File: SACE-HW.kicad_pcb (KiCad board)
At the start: 2 copper layers, 76 parts, among them IC201 1769205241, J201 Header_Male_Pin_2.54mm_1X2_,_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, J202 PJ-082BH, J301 Header_Male_Pin_2.54mm_1X6_,_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, J302 XH-4A connector, J401 1935161, J402 Header_Male_Pin_2.54mm_1X3_,_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, J403 RF1-01K-D-00-50-BK-HDW, J404 1935161, J501 690-005-299-043, Q401 MCB90N12A-TP, Q402 MCB90N12A-TP, SW301 PTS645SM43SMTR92, SW302 PTS645SM43SMTR92, U201 OKI-78SR-5_1.5-W36H-C, U202 AZ1117IH-3.3TRG1, U203 AZ1117IH-3.3TRG1, U301 STM32F446RE, U401 LTV-816S, U402 TMCS1108A4UQDR, U501 MCP2221A-I_SL

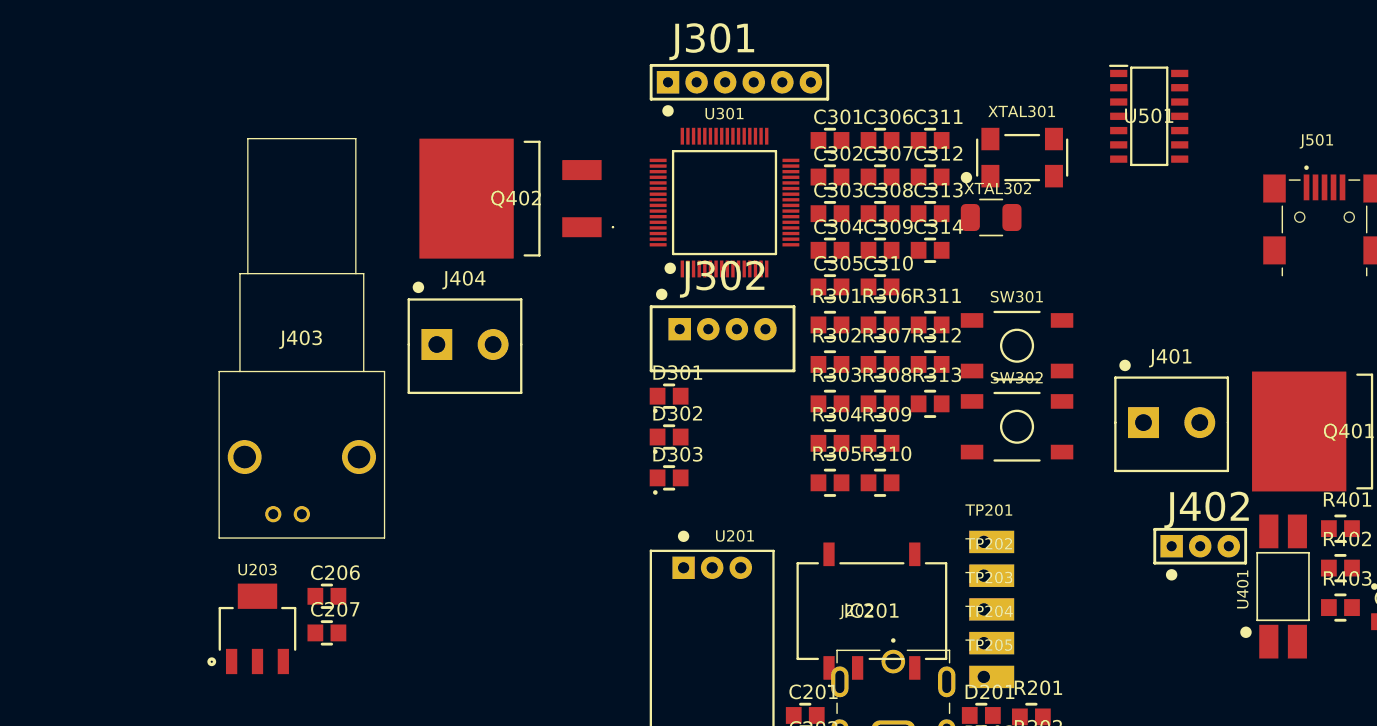
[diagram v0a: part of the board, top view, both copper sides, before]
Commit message: update schematic
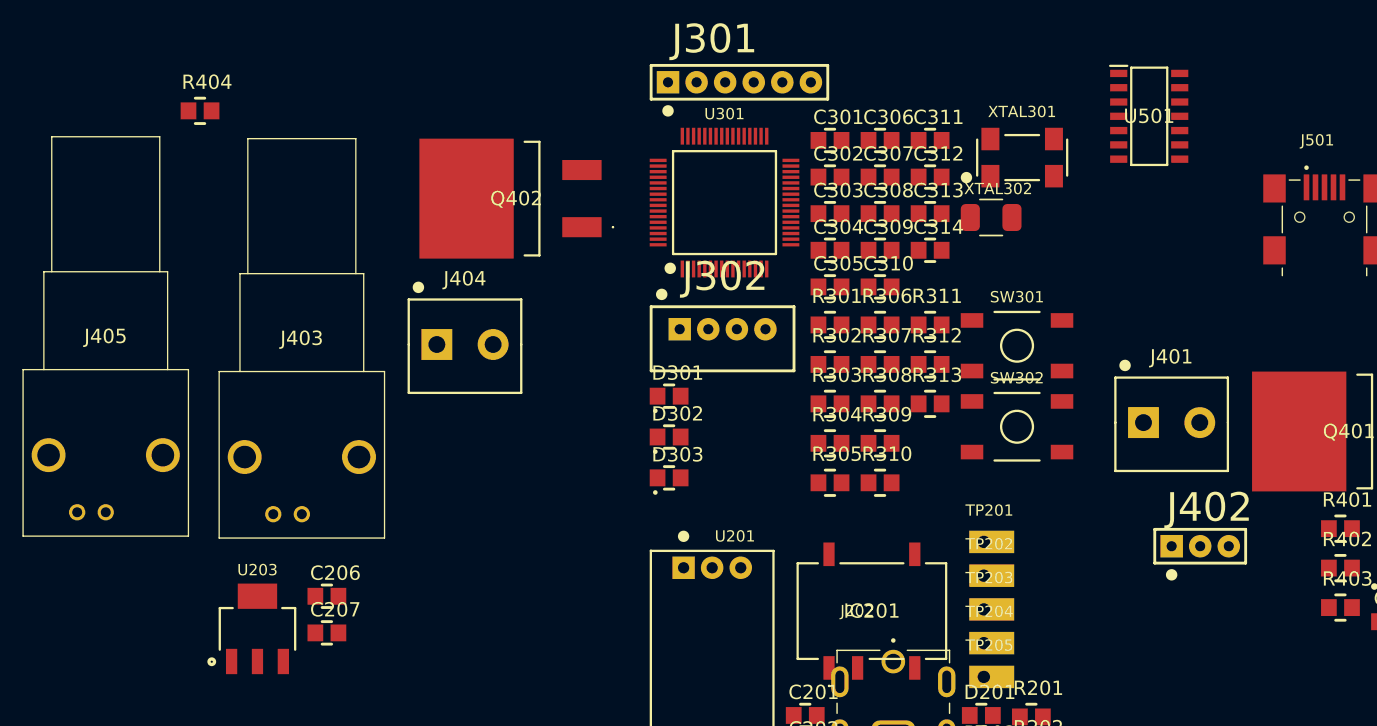
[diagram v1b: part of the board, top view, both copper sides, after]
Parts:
- removed U401: LTV-816S, IC:4-SMD
- added J405: RF1-01K-D-00-50-BK-HDW, Connectors:RF101KD0050, F.Cu at (65.2, 81.4)
- added R404: RC0805JR-071KL, Resistors:R0805, F.Cu at (72.6, 45.7)
- R401: value RC0805JR-071KL -> RC0805JR-07330RL
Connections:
- net Net-(U401-E) renamed /HV/pulse_gate
- C401 pad 2: 3.3VB -> 3.3VA
- J403 pad 2: Net-(Q402-D) -> GNDA
- J403 pad MH: Net-(Q402-D) -> GNDA
- J404 pad 1: Net-(Q402-D) -> GNDA
- Q401 pad 1: unconnected-(Q401-G-Pad1) -> Net-(Q401-G)
- Q402 pad 2: Net-(Q402-D) -> GNDA
- R401 pad 1: Net-(U401-Anode) -> /HV/boost_gate
- R401 pad 2: /HV/gate_drive -> Net-(Q401-G)
- U402 pad 5: GNDB -> GNDA
- U402 pad 8: 3.3VB -> 3.3VA
- U501 pad 5: /USB_Serial/UART_RX -> unconnected-(U501-URX-Pad5)
- U501 pad 6: /USB_Serial/UART_TX -> unconnected-(U501-UTX-Pad6)

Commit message: update schematic
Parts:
- removed U402: TMCS1108A4UQDR, IC:SOIC-8
- added C601: 885012107015, Capacitors:C0603, F.Cu at (160.4, 129.1)
- added C602: 885012107015, Capacitors:C0603, F.Cu at (160.4, 131.6)
- added C603: 885012107015, Capacitors:C0603, F.Cu at (160.4, 134.1)
- added D401: SBRD10200TR, Diodes:DPAK228P1005X240-4N, F.Cu at (91.2, 100.6)
- added J601: 2350514-8, Connectors:CONN8_2350514-8_TEC, F.Cu at (119.5, 127.0)
- added J602: XH-4A connector, Connectors:XH-4A, F.Cu at (162.7, 123.6)
- added J701: 2350514-8, Connectors:CONN8_2350514-8_TEC, F.Cu at (89.1, 127.0)
- added L401: ATCA-08-471M-H, Inductors:IND_ATCA-08-471M-H, F.Cu at (64.5, 116.8)
- added R601: RC0805JR-070RL, Resistors:R0603, F.Cu at (173.5, 129.2)
- added R602: RC0805JR-070RL, Resistors:R0603, F.Cu at (173.5, 131.9)
- added R603: RC0805JR-074K7L, Resistors:R0805, F.Cu at (164.1, 129.7)
- added R604: RC0805JR-074K7L, Resistors:R0805, F.Cu at (164.1, 133.2)
- added TP206: Test_Point_THM, Connectors:Keystone_5001, F.Cu at (151.4, 120.7)
- added U401: TMCS1108A4UQDR, IC:SOIC-8, F.Cu at (91.1, 111.6)
- added U601: TLA2528IRTER, IC:QFN50P300X300X80-17N-D, F.Cu at (170.0, 130.6)
- R402: value RC0805JR-07330RL -> RC0805JR-071KL
- R403: value RC0805JR-071KL -> RC0805JR-07330RL
- moved J202 29.7 mm to (164.2, 110.5)
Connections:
- J403 pad 2: GNDA -> /HV/electrode
- J403 pad MH: GNDA -> /HV/electrode
- J404 pad 1: GNDA -> /HV/electrode
- Q401 pad 2: unconnected-(Q401-D-Pad2) -> Net-(Q401-D)
- Q402 pad 2: GNDA -> /HV/electrode
- R402 pad 1: /HV/pulse_gate -> GNDA
- R402 pad 2: Net-(Q402-G) -> /HV/boost_gate
- R403 pad 1: GNDA -> /HV/pulse_gate
- R403 pad 2: /HV/pulse_gate -> Net-(Q402-G)
- R404 pad 2: /HV/boost_gate -> /HV/pulse_gate
- U501 pad 10: /USB_Serial/SCL -> unconnected-(U501-SCL-Pad10)
- U501 pad 9: /USB_Serial/SDA -> unconnected-(U501-SDA-Pad9)

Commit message: modif schématique
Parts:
- removed IC201: 1769205241, IC:1769205241
- added C208: 885012107014, Capacitors:C0805, F.Cu at (79.4, 125.4)
- added D204: 150080VS75000, Diodes:LED_0805_GREEN, F.Cu at (83.8, 135.5)
- added D205: 150080VS75000, Diodes:LED_0805_GREEN, F.Cu at (83.8, 139.1)
- added D206: 150080VS75000, Diodes:LED_0805_GREEN, F.Cu at (83.8, 142.8)
- added D402: SBRD10200TR, Diodes:DPAK228P1005X240-4N, F.Cu at (98.9, 81.9)
- added F202: 39511000440, Fuses:TE5_395, F.Cu at (98.7, 128.0)
- added J203: 1935161, Connectors:1935161, F.Cu at (88.2, 118.1)
- added R204: RC0805JR-0733KL, Resistors:R0805, F.Cu at (88.3, 135.3)
- added R205: RC0805FR-075K6L, Resistors:R0805, F.Cu at (88.3, 138.8)
- added R206: RC0805JR-072K2L, Resistors:R0805, F.Cu at (88.3, 142.3)
- added R405: RC0805FR-075K6L, Resistors:R0805, F.Cu at (74.4, 91.4)
- added R406: RC0805FR-07200KL, Resistors:R0805, F.Cu at (78.8, 77.3)
- added R407: RC0805JR-07330RL, Resistors:R0805, F.Cu at (78.8, 80.8)
- added R408: RC0805JR-071KL, Resistors:R0805, F.Cu at (78.8, 84.3)
- added R409: RC0805JR-071KL, Resistors:R0805, F.Cu at (78.8, 87.9)
- added R410: RC0805FR-075K6L, Resistors:R0805, F.Cu at (78.8, 91.4)
- added R411: RMCF0805FT10M0, Resistors:R0805, F.Cu at (83.3, 77.3)
- added R412: RC0805FR-075K6L, Resistors:R0805, F.Cu at (83.3, 80.8)
- added R413: RC0805FR-07200KL, Resistors:R0805, F.Cu at (83.3, 84.3)
- added R605: RC0805JR-071KL, Resistors:R0805, F.Cu at (157.1, 73.1)
- added R606: RC0805JR-070RL, Resistors:R0603, F.Cu at (180.5, 58.6)
- added R607: RC0805JR-070RL, Resistors:R0603, F.Cu at (180.5, 61.3)
- added TP207: Test_Point_THM, Connectors:Keystone_5001, F.Cu at (75.0, 120.5)
- added TP208: Test_Point_THM, Connectors:Keystone_5001, F.Cu at (75.0, 123.5)
- added TP209: Test_Point_THM, Connectors:Keystone_5001, F.Cu at (75.0, 126.5)
- added TP401: Test_Point_THM, Connectors:Keystone_5001, F.Cu at (114.2, 90.9)
- added U204: AZ1117IH-3.3TRG1, IC:SOT-223-3, F.Cu at (107.7, 134.8)
- added U402: LTV-816S, IC:4-SMD, F.Cu at (107.3, 82.5)
- added U403: TMCS1108A4UQDR, IC:SOIC-8, F.Cu at (99.0, 92.9)
- added U602: TCA9617BDGKR, IC:SOP65P490X110-8N, F.Cu at (164.6, 68.0)
- C205: value 885012107014 -> 885012107005
- C206: value 885012107005 -> 885012107018
- C207: value 885012107014 -> 885012107018
- J201: value Header_Male_Pin_2.54mm_1X2_,_Unshrouded -> 1935161; footprint Connectors:Headers_2.54mm_1X2 -> Connectors:1935161
- J202: value PJ-082BH -> Header_Male_Pin_2.54mm_1X2_,_Unshrouded; footprint Connectors:CUI_PJ-082BH -> Connectors:Headers_2.54mm_1X2
- J403: value RF1-01K-D-00-50-BK-HDW -> 1935161; footprint Connectors:RF101KD0050 -> Connectors:1935161
- J404: value 1935161 -> RF1-01K-D-00-50-BK-HDW; footprint Connectors:1935161 -> Connectors:RF101KD0050
- J601: value 2350514-8 -> XH-4A connector; footprint Connectors:CONN8_2350514-8_TEC -> Connectors:XH-4A
- J602: value XH-4A connector -> 2350514-8; footprint Connectors:XH-4A -> Connectors:CONN8_2350514-8_TEC
- R403: value RC0805JR-07330RL -> RMCF0805FT10M0
- R404: value RC0805JR-071KL -> RC0805FR-075K6L
- R601, R602: value RC0805JR-070RL -> RC0805JR-074K7L; footprint Resistors:R0603 -> Resistors:R0805
- U203: value AZ1117IH-3.3TRG1 -> OKI-78SR-5_1.5-W36H-C; footprint IC:SOT-223-3 -> Assembly:OKI-78SR_Horizontal
- U401: value TMCS1108A4UQDR -> MCP6L04T-E/SL; footprint IC:SOIC-8 -> IC:SOIC127P600X175-14N
- moved J701 127.9 mm to (183.6, 40.8), turned to 0 degrees
- moved R401 99.7 mm to (74.4, 77.3)
- moved R402 99.7 mm to (74.4, 80.8)
- moved R403 99.7 mm to (74.4, 84.3)
- moved J405 81.4 mm to (145.0, 65.4)
- moved J601 79.0 mm to (163.5, 61.4), turned to 0 degrees
- moved TP206 76.5 mm to (75.0, 117.5)
- moved R601 72.1 mm to (157.1, 59.0)
- moved J602 71.4 mm to (183.6, 55.3)
- moved R602 71.3 mm to (157.1, 62.5)
- moved L401 71.1 mm to (95.8, 53.0)
- moved U601 71.0 mm to (177.0, 60.0)
- moved TP201 70.8 mm to (75.0, 102.5)
- moved TP202 70.8 mm to (75.0, 105.5)
- moved TP203 70.8 mm to (75.0, 108.5)
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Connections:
- C202 pad 2: Net-(TP203-TP) -> Net-(TP202-TP)
- C205 pad 1: GNDA -> GNDB
- C205 pad 2: Net-(J202-SHIELD) -> 3.3VB
- C206 pad 2: 3.3VB -> Net-(TP207-TP)
- C401 pad 1: GNDB -> GNDA
- C603 pad 2: /GPIO/decap -> /5V_LOGIC_I2C/decap
- F201 pad 2: Net-(TP203-TP) -> Net-(TP202-TP)
- J201 pad 1: 3.3VA -> GNDA
- J201 pad 2: VDD -> 12VA
- J202 pad 1: 12VA -> 3.3VB
- J202 pad 2: GNDA -> VDD
- J403 pad 1: HV -> /HV/e-
- J403 pad 2: /HV/electrode -> HV
- J404 pad 1: /HV/electrode -> /HV/V_amp
- J404 pad 2: HV -> GNDA
- J601 pad 1: Net-(U601-AIN0/GPIO0) -> GNDB
- J601 pad 2: Net-(U601-AIN1/GPIO1) -> /5V_LOGIC_I2C/SDA
- J601 pad 3: Net-(U601-AIN2/GPIO2) -> /5V_LOGIC_I2C/SCL
- J601 pad 4: Net-(U601-AIN3/GPIO3) -> 5VB
- J602 pad 1: GNDB -> Net-(U601-AIN0/GPIO0)
- J602 pad 2: /GPIO/SDA -> Net-(U601-AIN1/GPIO1)
- J602 pad 3: /GPIO/SCL -> Net-(U601-AIN2/GPIO2)
- J602 pad 4: 5VB -> Net-(U601-AIN3/GPIO3)
- Q402 pad 2: /HV/electrode -> /HV/e-
- R201 pad 2: Net-(TP203-TP) -> Net-(TP202-TP)
- R403 pad 1: /HV/pulse_gate -> Net-(R403-Pad1)
- R403 pad 2: Net-(Q402-G) -> HV
- R404 pad 1: GNDA -> Net-(R404-Pad1)
- R404 pad 2: /HV/pulse_gate -> GNDA
- R601 pad 1: /GPIO/decap -> /5V_LOGIC_I2C/SCL_5
- R601 pad 2: Net-(U601-ADDR) -> 5VB
- R602 pad 1: Net-(U601-ADDR) -> /5V_LOGIC_I2C/SDA_5
- R602 pad 2: GNDB -> 5VB
- R603 pad 1: /GPIO/SCL -> /5V_LOGIC_I2C/SCL_3_3
- R603 pad 2: 5VB -> 3.3VB
- R604 pad 1: /GPIO/SDA -> /5V_LOGIC_I2C/SDA_3_3
- R604 pad 2: 5VB -> 3.3VB
- TP202 pad 1: VDD -> Net-(TP202-TP)
- TP203 pad 1: Net-(TP203-TP) -> 5VA
- TP204 pad 1: 5VA -> GNDA
- TP205 pad 1: GNDA -> 3.3VB
- TP206 pad 1: GNDB -> VDD
- U201 pad 1: Net-(TP203-TP) -> Net-(TP202-TP)
- U203 pad 1: GNDB -> Net-(TP207-TP)
- U203 pad 2: 3.3VB -> GNDB
- U401 pad 1: Net-(Q402-S) -> Net-(R405-Pad1)
- U401 pad 2: Net-(Q402-S) -> Net-(R405-Pad1)
- U401 pad 3: GNDA -> Net-(R403-Pad1)
- U401 pad 4: GNDA -> 3.3VA
- U401 pad 5: GNDA -> Net-(R411-Pad1)
- U401 pad 6: unconnected-(U401-NC-Pad6) -> Net-(R412-Pad1)
- U401 pad 7: /HV/current_sense -> Net-(R412-Pad1)
- U401 pad 8: 3.3VA -> /HV/V_amp
- U601 pad 13: /GPIO/SCL -> /5V_LOGIC_I2C/SCL_5
- U601 pad 14: /GPIO/SDA -> /5V_LOGIC_I2C/SDA_5
- U601 pad 8: /GPIO/decap -> /5V_LOGIC_I2C/decap

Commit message: update schematique
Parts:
- added C24: 885012207098, Capacitors:C0805, F.Cu at (180.5, 105.7)
- added C25: 885012207098, Capacitors:C0805, F.Cu at (180.5, 109.0)
- added D12: 150080VS75000, Diodes:LED_0805_GREEN, F.Cu at (176.1, 105.7)
- added D13: 150080YS75000, Diodes:LED_0805_YELLOW, F.Cu at (176.1, 109.4)
- added J12: Header_Male_Pin_2.54mm_1X4_,_Unshrouded, Connectors:Headers_2.54mm_1X4, F.Cu at (177.0, 100.6)
- added R23: RC0805JR-071KL, Resistors:R0805, F.Cu at (178.8, 116.2)
- added R24: RC0805JR-071KL, Resistors:R0805, F.Cu at (178.8, 119.7)
- added R35: RC0805JR-072K2L, Resistors:R0805, F.Cu at (171.6, 100.2)
- added R36: RC0805JR-072K2L, Resistors:R0805, F.Cu at (171.6, 103.7)
- added SB1: Solder_Bridge, Connectors:Solder_bridge_0805, F.Cu at (172.7, 107.2)
- added SB2: Solder_Bridge, Connectors:Solder_bridge_0805, F.Cu at (172.7, 110.7)
- added U8: LTV-816S, IC:4-SMD, F.Cu at (174.8, 121.4)
- renumbered C202 to C1, C311 to C10, C306 to C11, C302 to C12, C308 to C13, C309 to C14, C303 to C15, C304 to C16, C314 to C17, C301 to C18, C312 to C19, C206 to C2, C313 to C20, C307 to C21, C310 to C22, C401 to C23, C601 to C26, C602 to C27, C603 to C28, C203 to C3, C207 to C4, C204 to C5, C208 to C6, C201 to C7, C205 to C8, C305 to C9, D201 to D1, D401 to D10, D402 to D11, D204 to D2, D202 to D3, D205 to D4, D203 to D5, D206 to D6, D301 to D7, D302 to D8, D303 to D9, F201 to F1, F202 to F2, J201 to J1, J403 to J10, J501 to J11, J601 to J13, J602 to J14, J701 to J15, J203 to J2, J202 to J3, J302 to J4, J301 to J5, J401 to J6, J402 to J7, J404 to J8, J405 to J9, L401 to L1, Q402 to Q1, Q401 to Q2, R201 to R1, R309 to R10, R308 to R11, R313 to R12, R302 to R13, R310 to R14, R311 to R15, R301 to R16, R312 to R17, R306 to R18, R304 to R19, R204 to R2, R408 to R20, R409 to R21, R407 to R22, R402 to R25, R401 to R26, R403 to R27, R406 to R28, R411 to R29, R202 to R3, R413 to R30, R405 to R31, R412 to R32, R404 to R33, R410 to R34, R606 to R37, R607 to R38, R601 to R39, R205 to R4, R602 to R40, R203 to R5, R206 to R6, R305 to R7, R303 to R8, R307 to R9, SW302 to SW1, SW301 to SW2, TP202 to TP1, TP401 to TP10, TP207 to TP2, TP204 to TP3, TP209 to TP4, TP203 to TP5, TP208 to TP6, TP201 to TP7, TP205 to TP8, TP206 to TP9, U201 to U1, U501 to U10, U601 to U11, U203 to U2, U202 to U3, U204 to U4, U301 to U5, U402 to U6, U403 to U7, U401 to U9, XTAL302 to XTAL1, XTAL301 to XTAL2
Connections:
- net /5V_LOGIC_I2C/decap renamed /I2C/decap
- net /HV/boost_gate renamed Net-(U8-E)
- J11 pad 1: unconnected-(J501-VCC-Pad1) -> /USB_Serial/USB_VBUS
- J11 pad 4: unconnected-(J501-ID-Pad4) -> Net-(J11-ID)
- J13 pad 2: /5V_LOGIC_I2C/SDA -> /I2C/SDA
- J13 pad 3: /5V_LOGIC_I2C/SCL -> /I2C/SCL
- R39 pad 1: /5V_LOGIC_I2C/SCL_5 -> /I2C/SCL
- R40 pad 1: /5V_LOGIC_I2C/SDA_5 -> /I2C/SDA
- U10 pad 1: unconnected-(U501-VDD-Pad1) -> 3.3VB
- U10 pad 10: unconnected-(U501-SCL-Pad10) -> /USB_Serial/SCL
- U10 pad 11: unconnected-(U501-VUSB-Pad11) -> Net-(U10-VUSB)
- U10 pad 2: unconnected-(U501-GP0-Pad2) -> /USB_Serial/GP0
- U10 pad 3: unconnected-(U501-GP1-Pad3) -> /USB_Serial/GP1
- U10 pad 4: unconnected-(U501-~{RST}-Pad4) -> /USB_Serial/RST_
- U10 pad 5: unconnected-(U501-URX-Pad5) -> /USB_Serial/UART_RX
- U10 pad 6: unconnected-(U501-UTX-Pad6) -> /USB_Serial/UART_TX
- U10 pad 7: unconnected-(U501-GP2-Pad7) -> /USB_Serial/GP2
- U10 pad 8: unconnected-(U501-GP3-Pad8) -> /USB_Serial/GP3
- U10 pad 9: unconnected-(U501-SDA-Pad9) -> /USB_Serial/SDA
- U11 pad 13: /5V_LOGIC_I2C/SCL_5 -> /I2C/SCL
- U11 pad 14: /5V_LOGIC_I2C/SDA_5 -> /I2C/SDA
- U6 pad 4: 3.3VA -> 5VA

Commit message: update schematique
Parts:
- removed C1, C19, C2, C3, C4: 885012107018, Capacitors:C0805
- removed C10, C17, C18, C20, C21, C22, C23, C24, C25: 885012207098, Capacitors:C0805
- removed C11, C9: 885012007053, Capacitors:C0805
- removed C12, C15: 885012007027, Capacitors:C0805
- removed C13, C16: 885012107015, Capacitors:C0805
- removed C14: 885012207092, Capacitors:C0805
- removed C26, C27, C28: 885012107015, Capacitors:C0603
- removed C5, C6: 885012107014, Capacitors:C0805
- removed C7, C8: 885012107005, Capacitors:C0805
- removed D1, D12, D2, D3, D4, D5, D6, D7: 150080VS75000, Diodes:LED_0805_GREEN
- removed D10, D11: SBRD10200TR, Diodes:DPAK228P1005X240-4N
- removed D13, D8: 150080YS75000, Diodes:LED_0805_YELLOW
- removed D9: 150080RS75000, Diodes:LED_0805_RED
- removed F1, F2: 39511000440, Fuses:TE5_395
- removed J1, J10, J2, J6: 1935161, Connectors:1935161
- removed J11: 690-005-299-043, Connectors:EDAC_690-005-299-043
- removed J12: Header_Male_Pin_2.54mm_1X4_,_Unshrouded, Connectors:Headers_2.54mm_1X4
- removed J13, J4: XH-4A connector, Connectors:XH-4A
- removed J14, J15: 2350514-8, Connectors:CONN8_2350514-8_TEC
- removed J3: Header_Male_Pin_2.54mm_1X2_,_Unshrouded, Connectors:Headers_2.54mm_1X2
- removed J5: Header_Male_Pin_2.54mm_1X6_,_Unshrouded, Connectors:Headers_2.54mm_1X6
- removed J7: Header_Male_Pin_2.54mm_1X3_,_Unshrouded, Connectors:Headers_2.54mm_1X3
- removed J8, J9: RF1-01K-D-00-50-BK-HDW, Connectors:RF101KD0050
- removed L1: ATCA-08-471M-H, Inductors:IND_ATCA-08-471M-H
- removed Q1, Q2: MCB90N12A-TP, IC:MCB90N12ATP
- removed R1, R2: RC0805JR-0733KL, Resistors:R0805
- removed R10, R11: RC0805JR-07470RL, Resistors:R0805
- removed R12, R14, R15, R17, R35, R36, R5, R6: RC0805JR-072K2L, Resistors:R0805
- removed R13, R8: RC0805JR-070RL, Resistors:R0805
- removed R16: RC0805JR-0710KL, Resistors:R0805
- removed R18, R9: RC0805JR-07150RL, Resistors:R0805
- removed R19, R39, R40, R7: RC0805JR-074K7L, Resistors:R0805
- removed R20, R21, R23, R24, R25: RC0805JR-071KL, Resistors:R0805
- removed R22, R26: RC0805JR-07330RL, Resistors:R0805
- removed R27, R29: RMCF0805FT10M0, Resistors:R0805
- removed R28, R30: RC0805FR-07200KL, Resistors:R0805
- removed R3, R31, R32, R33, R34, R4: RC0805FR-075K6L, Resistors:R0805
- removed R37, R38: RC0805JR-070RL, Resistors:R0603
- removed SB1, SB2: Solder_Bridge, Connectors:Solder_bridge_0805
- removed SW1, SW2: PTS645SM43SMTR92, Switches:PTS645_6X6X4_SMD
- removed TP1, TP10, TP2, TP3, TP4, TP5, TP6, TP7, TP8, TP9: Test_Point_THM, Connectors:Keystone_5001
- removed U1, U2: OKI-78SR-5_1.5-W36H-C, Assembly:OKI-78SR_Horizontal
- removed U10: MCP2221A-I_SL, IC:SOIC127P600X175-14N
- removed U11: TLA2528IRTER, IC:QFN50P300X300X80-17N-D
- removed U3, U4: AZ1117IH-3.3TRG1, IC:SOT-223-3
- removed U5: STM32F446RE, IC:LQFP-64
- removed U6, U8: LTV-816S, IC:4-SMD
- removed U7: TMCS1108A4UQDR, IC:SOIC-8
- removed U9: MCP6L04T-E/SL, IC:SOIC127P600X175-14N
- removed XTAL1: 7A-8.000MAHJ-T, Crystals:TXC_7A_Series
- removed XTAL2: ABS25-32.768KHZ-6-T, Crystals:ABS25
- added C201: 885012107005, Capacitors:C0805, F.Cu at (95.0, 82.8)
- added C202: 885012107014, Capacitors:C0805, F.Cu at (95.0, 86.0)
- added C203: 885012107005, Capacitors:C0805, F.Cu at (95.0, 89.3)
- added C204: 885012107018, Capacitors:C0805, F.Cu at (95.0, 92.5)
- added C205: 885012107018, Capacitors:C0805, F.Cu at (95.0, 95.8)
- added C206: 885012107014, Capacitors:C0805, F.Cu at (95.0, 99.0)
- added C301: 885012207098, Capacitors:C0805, F.Cu at (77.9, 125.3)
- added C302: 885012007027, Capacitors:C0805, F.Cu at (77.9, 128.6)
- added C303: 885012007027, Capacitors:C0805, F.Cu at (77.9, 131.8)
- added C304: 885012107015, Capacitors:C0805, F.Cu at (77.9, 135.1)
- added C305: 885012007053, Capacitors:C0805, F.Cu at (77.9, 138.3)
- added C306: 885012007053, Capacitors:C0805, F.Cu at (82.4, 125.3)
- added C307: 885012207098, Capacitors:C0805, F.Cu at (82.4, 128.6)
- added C308: 885012107015, Capacitors:C0805, F.Cu at (82.4, 131.8)
- added C309: 885012207092, Capacitors:C0805, F.Cu at (82.4, 135.1)
- added C310: 885012207098, Capacitors:C0805, F.Cu at (82.4, 138.3)
- added C311: 885012207098, Capacitors:C0805, F.Cu at (86.8, 125.3)
- added C312: 885012107018, Capacitors:C0805, F.Cu at (86.8, 128.6)
- added C313: 885012207098, Capacitors:C0805, F.Cu at (86.8, 131.8)
- added C314: 885012207098, Capacitors:C0805, F.Cu at (86.8, 135.1)
- added C401: 885012207098, Capacitors:C0805, F.Cu at (64.5, 117.3)
- added C402: 885012207103, Capacitors:C0805, F.Cu at (64.5, 120.6)
- added C403: 885012207098, Capacitors:C0805, F.Cu at (64.5, 123.8)
- added C404: 885012207103, Capacitors:C0805, F.Cu at (64.5, 127.1)
- added C501: 885012207098, Capacitors:C0805, F.Cu at (135.6, 87.8)
- added C502: 885012207098, Capacitors:C0805, F.Cu at (135.6, 91.0)
- added C601: 885012107015, Capacitors:C0603, F.Cu at (108.4, 20.9)
- added C602: 885012107015, Capacitors:C0603, F.Cu at (108.4, 23.4)
- added C603: 885012107015, Capacitors:C0603, F.Cu at (108.4, 25.8)
- added C604: 885012107015, Capacitors:C0603, F.Cu at (108.4, 28.3)
- added C605: 885012107015, Capacitors:C0603, F.Cu at (108.4, 30.7)
- added C606: 885012107015, Capacitors:C0603, F.Cu at (108.4, 33.2)
- added C607: 885012107015, Capacitors:C0603, F.Cu at (108.4, 35.7)
- added C608: 885012107015, Capacitors:C0603, F.Cu at (108.4, 38.1)
- added C701: 885012207098, Capacitors:C0805, F.Cu at (29.5, 145.6)
- added C702: 885012207098, Capacitors:C0805, F.Cu at (29.5, 148.8)
- added C801: 885012107015, Capacitors:C0805, F.Cu at (137.4, 132.3)
- added C802: 885012207098, Capacitors:C0805, F.Cu at (137.4, 135.6)
- added C803: 885012207098, Capacitors:C0805, F.Cu at (137.4, 138.8)
- added D201: 150080VS75000, Diodes:LED_0805_GREEN, F.Cu at (99.5, 82.8)
- added D202: 150080VS75000, Diodes:LED_0805_GREEN, F.Cu at (99.5, 86.4)
- added D203: 150080VS75000, Diodes:LED_0805_GREEN, F.Cu at (99.5, 90.0)
- added D204: 150080VS75000, Diodes:LED_0805_GREEN, F.Cu at (99.5, 93.7)
- added D205: 150080VS75000, Diodes:LED_0805_GREEN, F.Cu at (99.5, 97.3)
- added D301: 150080VS75000, Diodes:LED_0805_GREEN, F.Cu at (91.3, 139.7)
- added D302: 150080YS75000, Diodes:LED_0805_YELLOW, F.Cu at (91.3, 143.3)
- added D303: 150080RS75000, Diodes:LED_0805_RED, F.Cu at (91.3, 147.0)
- added D501: 150080VS75000, Diodes:LED_0805_GREEN, F.Cu at (131.1, 87.8)
- added D502: 150080YS75000, Diodes:LED_0805_YELLOW, F.Cu at (131.1, 91.4)
- added D901: DSS16U, Diodes:SOD-123FL, F.Cu at (65.1, 56.3)
- added D902: DSS16U, Diodes:SOD-123FL, F.Cu at (65.1, 60.5)
- added D903: DSS16U, Diodes:SOD-123FL, F.Cu at (65.1, 64.8)
- added D904: DSS16U, Diodes:SOD-123FL, F.Cu at (65.1, 69.0)
- added F201: 39511000440, Fuses:TE5_395, F.Cu at (86.6, 103.4)
- added H101: Mounting-Hole-M3, Connectors:Mounting_Hole_3mm, F.Cu at (175.5, 28.8)
- added H102: Mounting-Hole-M3, Connectors:Mounting_Hole_3mm, F.Cu at (265.5, 28.8)
- added H103: Mounting-Hole-M3, Connectors:Mounting_Hole_3mm, F.Cu at (175.5, 118.8)
- added H104: Mounting-Hole-M3, Connectors:Mounting_Hole_3mm, F.Cu at (265.5, 118.8)
- added IC201: 1769205241, IC:1769205241, F.Cu at (115.3, 97.8)
- added J201: Header_Male_Pin_2.54mm_1X2_,_Unshrouded, Connectors:Headers_2.54mm_1X2, F.Cu at (109.3, 107.6)
- added J202: 1935161, Connectors:1935161, F.Cu at (113.1, 74.8)
- added J203: 2350514-8, Connectors:CONN8_2350514-8_TEC, F.Cu at (104.4, 79.1)
- added J301: Header_Male_Pin_2.54mm_1X6_,_Unshrouded, Connectors:Headers_2.54mm_1X6, F.Cu at (96.7, 115.3)
- added J302: XH-4A connector, Connectors:XH-4A, F.Cu at (104.2, 142.1)
- added J401: 1935161, Connectors:1935161, F.Cu at (61.2, 97.2)
- added J402: 1935161, Connectors:1935161, F.Cu at (61.2, 108.2)
- added J403: RF1-01K-D-00-50-BK-HDW, Connectors:RF101KD0050, F.Cu at (28.9, 112.0)
- added J404: RF1-01K-D-00-50-BK-HDW, Connectors:RF101KD0050, F.Cu at (46.7, 112.0)
- added J501: Header_Male_Pin_2.54mm_1X4_,_Unshrouded, Connectors:Headers_2.54mm_1X4, F.Cu at (132.1, 82.6)
- added J502: 690-005-299-043, Connectors:EDAC_690-005-299-043, F.Cu at (131.7, 73.8)
- added J601: XH-4A connector, Connectors:XH-4A, F.Cu at (110.7, 43.4)
- added J602: XH-4A connector, Connectors:XH-4A, F.Cu at (110.7, 51.9)
- added J603: 2350514-8, Connectors:CONN8_2350514-8_TEC, F.Cu at (104.4, 30.1)
- added J604: 2350514-8, Connectors:CONN8_2350514-8_TEC, F.Cu at (104.4, 42.5)
- added J605: 2350514-8, Connectors:CONN8_2350514-8_TEC, F.Cu at (104.4, 55.0)
- added J701: 2350514-8, Connectors:CONN8_2350514-8_TEC, F.Cu at (47.6, 141.9)
- added J801: MEM2075-00-140-01-A, Connectors:GCT_MEM2075-00-140-01-A, F.Cu at (126.3, 126.4)
- added J901: 2350514-8, Connectors:CONN8_2350514-8_TEC, F.Cu at (71.6, 30.1)
- added J902: 2350514-8, Connectors:CONN8_2350514-8_TEC, F.Cu at (71.6, 42.5)
- added Q401: MCB90N12A-TP, IC:MCB90N12ATP, F.Cu at (27.7, 122.6)
- added Q901: PMV20XNER, IC:SOT-23-3, F.Cu at (46.7, 46.9)
- added Q902: PMV20XNER, IC:SOT-23-3, F.Cu at (46.7, 51.5)
- added Q903: PMV20XNER, IC:SOT-23-3, F.Cu at (51.5, 46.9)
- added Q904: PMV20XNER, IC:SOT-23-3, F.Cu at (51.5, 51.5)
- added Q905: PMV20XNER, IC:SOT-23-3, F.Cu at (56.4, 46.9)
- added Q906: PMV20XNER, IC:SOT-23-3, F.Cu at (56.4, 51.5)
- added Q907: PMV20XNER, IC:SOT-23-3, F.Cu at (61.2, 46.9)
- added Q908: PMV20XNER, IC:SOT-23-3, F.Cu at (61.2, 51.5)
- added R201: RC0805FR-075K6L, Resistors:R0805, F.Cu at (103.9, 91.9)
- added R202: RC0805JR-072K2L, Resistors:R0805, F.Cu at (103.9, 95.5)
- added R203: RC0805JR-0733KL, Resistors:R0805, F.Cu at (103.9, 99.0)
- added R204: RC0805FR-075K6L, Resistors:R0805, F.Cu at (103.9, 102.5)
- added R205: RC0805JR-072K2L, Resistors:R0805, F.Cu at (103.9, 106.0)
- added R301: RC0805JR-0710KL, Resistors:R0805, F.Cu at (77.9, 114.9)
- added R302: RC0805JR-070RL, Resistors:R0805, F.Cu at (77.9, 118.4)
- added R303: RC0805JR-070RL, Resistors:R0805, F.Cu at (77.9, 121.9)
- added R304: RC0805JR-074K7L, Resistors:R0805, F.Cu at (82.4, 114.9)
- added R305: RC0805JR-074K7L, Resistors:R0805, F.Cu at (82.4, 118.4)
- added R306: RC0805JR-07150RL, Resistors:R0805, F.Cu at (82.4, 121.9)
- added R307: RC0805JR-07150RL, Resistors:R0805, F.Cu at (86.8, 114.9)
- added R308: RC0805JR-07470RL, Resistors:R0805, F.Cu at (86.8, 118.4)
- added R309: RC0805JR-07470RL, Resistors:R0805, F.Cu at (86.8, 121.9)
- added R310: RC0805JR-072K2L, Resistors:R0805, F.Cu at (91.3, 114.9)
- added R311: RC0805JR-072K2L, Resistors:R0805, F.Cu at (91.3, 118.4)
- added R312: RC0805JR-072K2L, Resistors:R0805, F.Cu at (91.3, 121.9)
- added R401: RC0805JR-07330RL, Resistors:R0805, F.Cu at (56.8, 78.9)
- added R402: RC0805JR-072K2L, Resistors:R0805, F.Cu at (56.8, 82.4)
- added R403: RC0805FR-075K6L, Resistors:R0805, F.Cu at (56.8, 85.9)
- added R404: RMCF0805FT10M0, Resistors:R0805, F.Cu at (56.8, 89.4)
- added R405: RC0805FR-075K6L, Resistors:R0805, F.Cu at (61.2, 78.9)
- added R406: RC0805FR-075K6L, Resistors:R0805, F.Cu at (61.2, 82.4)
- added R407: RC0805FR-07200KL, Resistors:R0805, F.Cu at (61.2, 85.9)
- added R408: RC0805FR-075K6L, Resistors:R0805, F.Cu at (61.2, 89.4)
- added R409: RMCF0805FT10M0, Resistors:R0805, F.Cu at (65.7, 78.9)
- added R410: RC0805FR-075K6L, Resistors:R0805, F.Cu at (65.7, 82.4)
- added R411: RC0805FR-07200KL, Resistors:R0805, F.Cu at (65.7, 85.9)
- added R501: RC0805JR-072K2L, Resistors:R0805, F.Cu at (126.7, 82.2)
- added R502: RC0805JR-072K2L, Resistors:R0805, F.Cu at (126.7, 85.7)
- added R601: RC0805JR-074K7L, Resistors:R0805, F.Cu at (108.7, 57.9)
- added R602: RC0805JR-074K7L, Resistors:R0805, F.Cu at (108.7, 61.5)
- added R606: RC0805JR-0710KL, Resistors:R0805, F.Cu at (113.1, 57.9)
- added R607: RC0805JR-0710KL, Resistors:R0805, F.Cu at (113.1, 61.5)
- added R608: RC0805JR-07100KL, Resistors:R0805, F.Cu at (113.1, 65.0)
- added R609: RC0805JR-072K2L, Resistors:R0805, F.Cu at (117.6, 57.9)
- added R610: RC0805JR-070RL, Resistors:R0603, F.Cu at (117.0, 26.3)
- added R611: RC0805JR-0710KL, Resistors:R0805, F.Cu at (117.6, 61.5)
- added R612: RC0805JR-0710KL, Resistors:R0805, F.Cu at (117.6, 65.0)
- added R801: RC0805FR-0747KL, Resistors:R0805, F.Cu at (137.4, 114.9)
- added R802: RC0805JR-07150RL, Resistors:R0805, F.Cu at (137.4, 118.4)
- added R803: RC0805FR-0747KL, Resistors:R0805, F.Cu at (137.4, 121.9)
- added R804: RC0805FR-0747KL, Resistors:R0805, F.Cu at (137.4, 125.4)
- added R805: RC0805FR-0747KL, Resistors:R0805, F.Cu at (137.4, 128.9)
- added R806: RC0805FR-0747KL, Resistors:R0805, F.Cu at (141.8, 114.9)
- added R807: RC0805FR-0747KL, Resistors:R0805, F.Cu at (141.8, 118.4)
- added R901: RC0805JR-07330RL, Resistors:R0805, F.Cu at (45.2, 55.5)
- added R902: RC0805JR-07330RL, Resistors:R0805, F.Cu at (45.2, 59.0)
- added R903: RC0805JR-07330RL, Resistors:R0805, F.Cu at (45.2, 62.5)
- added R904: RC0805JR-07330RL, Resistors:R0805, F.Cu at (45.2, 66.0)
- added R905: RC0805JR-0710KL, Resistors:R0805, F.Cu at (49.6, 55.5)
- added R906: RC0805JR-0710KL, Resistors:R0805, F.Cu at (49.6, 59.0)
- added R907: RC0805JR-0710KL, Resistors:R0805, F.Cu at (49.6, 62.5)
- added R908: RC0805JR-0710KL, Resistors:R0805, F.Cu at (49.6, 66.0)
- added R909: RC0805JR-07330RL, Resistors:R0805, F.Cu at (54.1, 55.5)
- added R910: RC0805JR-07330RL, Resistors:R0805, F.Cu at (54.1, 59.0)
- added R911: RC0805JR-07330RL, Resistors:R0805, F.Cu at (54.1, 62.5)
- added R912: RC0805JR-07330RL, Resistors:R0805, F.Cu at (54.1, 66.0)
- added R913: RC0805JR-0710KL, Resistors:R0805, F.Cu at (58.5, 55.5)
- added R914: RC0805JR-0710KL, Resistors:R0805, F.Cu at (58.5, 59.0)
- added R915: RC0805JR-0710KL, Resistors:R0805, F.Cu at (58.5, 62.5)
- added R916: RC0805JR-0710KL, Resistors:R0805, F.Cu at (58.5, 66.0)
- added RL901: ALQ312, Relays:ALQ312, F.Cu at (32.0, 26.6)
- added RL902: ALQ312, Relays:ALQ312, F.Cu at (32.0, 40.5)
- added RL903: ALQ312, Relays:ALQ312, F.Cu at (32.0, 54.3)
- added RL904: ALQ312, Relays:ALQ312, F.Cu at (32.0, 68.2)
- added SB501: Solder_Bridge, Connectors:Solder_bridge_0805, F.Cu at (127.7, 89.2)
- added SB502: Solder_Bridge, Connectors:Solder_bridge_0805, F.Cu at (127.7, 92.7)
- added SB801: Solder_Bridge, Connectors:Solder_bridge_0805, F.Cu at (142.8, 121.9)
- added SB802: Solder_Bridge, Connectors:Solder_bridge_0805, F.Cu at (142.8, 125.4)
- added SB803: Solder_Bridge, Connectors:Solder_bridge_0805, F.Cu at (142.8, 128.9)
- added SB804: Solder_Bridge, Connectors:Solder_bridge_0805, F.Cu at (147.3, 114.9)
- added SB805: Solder_Bridge, Connectors:Solder_bridge_0805, F.Cu at (147.3, 118.4)
- added SB806: Solder_Bridge, Connectors:Solder_bridge_0805, F.Cu at (147.3, 121.9)
- added SW301: PTS645SM43SMTR92, Switches:PTS645_6X6X4_SMD, F.Cu at (95.6, 127.3)
- added SW302: PTS645SM43SMTR92, Switches:PTS645_6X6X4_SMD, F.Cu at (95.6, 134.5)
- added TP201: Test_Point_THM, Connectors:Keystone_5001, F.Cu at (78.5, 82.6)
- added TP202: Test_Point_THM, Connectors:Keystone_5001, F.Cu at (78.5, 85.6)
- added TP203: Test_Point_THM, Connectors:Keystone_5001, F.Cu at (78.5, 88.6)
- added TP204: Test_Point_THM, Connectors:Keystone_5001, F.Cu at (78.5, 91.6)
- added TP205: Test_Point_THM, Connectors:Keystone_5001, F.Cu at (78.5, 94.6)
- added TP206: Test_Point_THM, Connectors:Keystone_5001, F.Cu at (78.5, 97.6)
- added TP207: Test_Point_THM, Connectors:Keystone_5001, F.Cu at (78.5, 100.6)
- added U201: AZ1117IH-3.3TRG1, IC:SOT-223-3, F.Cu at (107.7, 85.7)
- added U202: OKI-78SR-5_1.5-W36H-C, Assembly:OKI-78SR_Horizontal, F.Cu at (87.8, 84.9)
- added U203: AZ1117IH-3.3TRG1, IC:SOT-223-3, F.Cu at (116.6, 85.7)
- added U301: STM32F446RE, IC:LQFP-64, F.Cu at (108.2, 130.8)
- added U401: LTV-816S, IC:4-SMD, F.Cu at (60.4, 122.6)
- added U402: TMCS1101A3UQDT, IC:SOIC-8, F.Cu at (52.8, 119.9)
- added U403: MCP6L04T-E/SL, IC:SOIC127P600X175-14N, F.Cu at (44.6, 120.9)
- added U501: MCP2221A-I_SL, IC:SOIC127P600X175-14N, F.Cu at (146.0, 85.6)
- added U601: MCP4728T-E_UN, IC:SOP50P490X110-10N, F.Cu at (80.0, 59.1)
- added U603: TLV9302IDR, Assembly:IC8_TLV9302IDR_TEX, F.Cu at (115.1, 33.7)
- added U604: TLA2528IRTER, IC:QFN50P300X300X80-17N-D, F.Cu at (113.5, 27.7)
- added U701: 74LVC4245APW_118, IC:SOP65P640X110-24N, F.Cu at (24.1, 148.5)
- added XTAL301: ABS25-32.768KHZ-6-T, Crystals:ABS25, F.Cu at (82.7, 143.1)
- added XTAL302: 7A-8.000MAHJ-T, Crystals:TXC_7A_Series, F.Cu at (97.7, 140.3)
- R603, R604: value RC0805JR-074K7L -> RC0805JR-070RL; footprint Resistors:R0805 -> Resistors:R0603
- R605: value RC0805JR-071KL -> RC0805JR-072K2L
- U602: value TCA9617BDGKR -> TLA2528IRTER; footprint IC:SOP65P490X110-8N -> IC:QFN50P300X300X80-17N-D
- moved U602 68.5 mm to (113.5, 22.4)
- moved R604 61.0 mm to (117.0, 23.7)
- moved R603 60.3 mm to (117.0, 21.0)
- moved R605 49.1 mm to (108.7, 65.0)
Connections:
- R603 pad 1: /5V_LOGIC_I2C/SCL_3_3 -> /I2C/decap
- R603 pad 2: 3.3VB -> Net-(U602-ADDR)
- R604 pad 1: /5V_LOGIC_I2C/SDA_3_3 -> Net-(U602-ADDR)
- R604 pad 2: 3.3VB -> GNDB
- R605 pad 1: 3.3VB -> GNDB
- R605 pad 2: Net-(U602-EN) -> /I2C/OUTA_12V
- U602 pad 1: 3.3VB -> Net-(U602-AIN2/GPIO2)
- U602 pad 2: /5V_LOGIC_I2C/SCL_3_3 -> Net-(U602-AIN3/GPIO3)
- U602 pad 3: /5V_LOGIC_I2C/SDA_3_3 -> Net-(U602-AIN4/GPIO4)
- U602 pad 4: GNDB -> Net-(U602-AIN5/GPIO5)
- U602 pad 5: Net-(U602-EN) -> Net-(U602-AIN6/GPIO6)
- U602 pad 6: /5V_LOGIC_I2C/SDA_5 -> Net-(U602-AIN7/GPIO7)
- U602 pad 7: /5V_LOGIC_I2C/SCL_5 -> 5VB
- U602 pad 8: 5VB -> /I2C/decap
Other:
- board outline added: 100 x 100 mm
